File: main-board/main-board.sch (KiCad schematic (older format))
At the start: 83 parts, among them J1 C10418, J2 FH12-24S-0.5SH(55), J3 TF-01A, Q1 Q_NPN_BCE, Q2 Q_NPN_BCE, Q3 Q_NPN_BCE, Q4 DMG1012T, SW1 SW_DIP_x01, U1 ESP-32s, U2 HT7333-A, U3 CH340E, U4 DW06D, U5 IPS6404L-SQ-SPN, U6 SX1308, U7 RT9011-CMGJ6, U8 SN74LVC125ADBR

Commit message: refactor
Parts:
- removed BT1: Battery_Holder, water-lib:Battery-Holder-SMD, symbol water-lib:Battery_Holder
- removed C1, C2: 10uF, Capacitor_SMD:C_0805_2012Metric_Pad1.15x1.40mm_HandSolder, symbol Device:C
- removed C19: 1uF, Capacitor_SMD:C_0805_2012Metric_Pad1.15x1.40mm_HandSolder, symbol Device:C
- removed C3, C4, C5: 0.1uF, Capacitor_SMD:C_0805_2012Metric_Pad1.15x1.40mm_HandSolder, symbol Device:C
- removed C6, C7: 22uF, Capacitor_SMD:C_1206_3216Metric_Pad1.42x1.75mm_HandSolder, symbol Device:C
- removed D1, D2, D3, D4: LED, LED_SMD:LED_0805_2012Metric_Pad1.15x1.40mm_HandSolder, symbol Device:LED
- removed D5: D_Schottky, Diode_SMD:D_SMA_Handsoldering, symbol Device:D_Schottky
- removed F1: SMD0805-020-16V, Fuse:Fuse_0805_2012Metric_Pad1.15x1.40mm_HandSolder, symbol water-lib:SMD0805-020-16V
- removed J1: C10418, water-lib:C10418, symbol water-lib:C10418
- removed L1: 22uH, Inductor_SMD:L_Bourns-SRN6028, symbol Device:L
- removed Q1, Q2: Q_NPN_BCE, Package_TO_SOT_SMD:SOT-23, symbol Device:Q_NPN_BCE
- removed Q4: DMG1012T, water-lib:SOT-523, symbol Device:Q_NMOS_GDS
- removed R1, R2, R6: 1k, Resistor_SMD:R_0805_2012Metric_Pad1.15x1.40mm_HandSolder, symbol pspice:R
- removed R19, R20, R28, R7, R9: 10k, Resistor_SMD:R_0805_2012Metric_Pad1.15x1.40mm_HandSolder, symbol pspice:R
- removed R27: 27k, Resistor_SMD:R_0805_2012Metric_Pad1.15x1.40mm_HandSolder, symbol pspice:R
- removed R3, R4: 1k5, Resistor_SMD:R_0805_2012Metric_Pad1.15x1.40mm_HandSolder, symbol pspice:R
- removed R5: 100, Resistor_SMD:R_0805_2012Metric_Pad1.15x1.40mm_HandSolder, symbol pspice:R
- removed R8: 2k2, Resistor_SMD:R_0805_2012Metric_Pad1.15x1.40mm_HandSolder, symbol pspice:R
- removed U2: HT7333-A, Package_TO_SOT_SMD:SOT-89-3_Handsoldering, symbol water-lib:HT7333-A
- removed U3: CH340E, water-lib:CH340E-MSOP-10, symbol water-lib:CH340E
- removed U4: DW06D, Package_TO_SOT_SMD:SOT-23-6_Handsoldering, symbol water-lib:DW06D
- removed U6: SX1308, Package_TO_SOT_SMD:SOT-23-6_Handsoldering, symbol water-lib:SX1308
- renumbered C14 to C104, C16 to C105, C17 to C106, C18 to C107, C9 to C109, C15 to C110, C8 to C111, C10 to C112, C12 to C113, C11 to C114, C13 to C115, D6 to D102, H1 to H101, H2 to H102, H3 to H103, H4 to H104, J3 to J101, J2 to J102, Q3 to Q102, R14 to R106, R15 to R107, R21 to R108, R22 to R109, R23 to R110, R16 to R111, R24 to R112, R18 to R113, R25 to R116, R13 to R117, R26 to R118, R10 to R119, R11 to R120, R12 to R121, R17 to R122, SW1 to SW101, TP1 to TP101, TP2 to TP102, TP3 to TP103, TP4 to TP104, TP5 to TP105, TP6 to TP106, TP7 to TP107, U1 to U103, U8 to U104, U5 to U105, U7 to U106
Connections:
- net labels removed: CTS, D+, D-, RTS, USB_PWR
- wire segments 279 -> 175
- no-connect marks 9 -> 7
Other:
- moved on the sheet: C105, C106, J101, R108, TP101, TP102, TP103, TP104, TP105, TP106, TP107

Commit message: refactor
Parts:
- removed C105: 10uF, Capacitor_SMD:C_0805_2012Metric_Pad1.15x1.40mm_HandSolder, symbol Device:C
- removed C106, C107: 0.1uF, Capacitor_SMD:C_0805_2012Metric_Pad1.15x1.40mm_HandSolder, symbol Device:C
- removed J101: TF-01A, water-lib:TF-01A, symbol water-lib:TF-01A
- removed R108, R109, R110, R112: 3k3, Resistor_SMD:R_0805_2012Metric_Pad1.15x1.40mm_HandSolder, symbol pspice:R
- removed TP102: VBAT, TestPoint:TestPoint_Pad_D1.0mm, symbol Connector:TestPoint
- removed U104: SN74LVC125ADBR, Package_SO:TSSOP-14_4.4x5mm_P0.65mm, symbol water-lib:SN74LVC125ADBR
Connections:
- net labels removed: SD_CLK, SD_CMD, SD_D0, SD_D3, VBAT
- wire segments 175 -> 134
- no-connect marks 7 -> 6
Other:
- moved on the sheet: D102, H101, H102, H103, H104, Q102, R113, R116, R118, SW101, TP101, TP103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

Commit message: ALPHA 1
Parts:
- removed C109, C110, C112, C114: 1uF, Capacitor_SMD:C_0805_2012Metric_Pad1.15x1.40mm_HandSolder, symbol Device:C
- removed C113: 15pF, Capacitor_SMD:C_0805_2012Metric_Pad1.15x1.40mm_HandSolder, symbol Device:C
- removed C115: 0.1uF, Capacitor_SMD:C_0805_2012Metric_Pad1.15x1.40mm_HandSolder, symbol Device:C
- removed J102: FH12-24S-0.5SH(55), water-lib:FH12-24S-0.5SH(55), symbol water-lib:FH12-24S-0.5SH(55)
- removed R106, R107, R122: 4k7, Resistor_SMD:R_0805_2012Metric_Pad1.15x1.40mm_HandSolder, symbol pspice:R
- removed R111, R120, R121: 10k, Resistor_SMD:R_0805_2012Metric_Pad1.15x1.40mm_HandSolder, symbol pspice:R
- removed R117: 1k, Resistor_SMD:R_0805_2012Metric_Pad1.15x1.40mm_HandSolder, symbol pspice:R
- removed U106: RT9011-CMGJ6, Package_TO_SOT_SMD:SOT-23-6_Handsoldering, symbol water-lib:RT9011-CMGJ6
- SW101: value SW_DIP_x01 -> RESET
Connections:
- net labels removed: CAM_RST, CSI_PWD
- wire segments 134 -> 90
- no-connect marks 6 -> 3
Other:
- moved on the sheet: C104, C111, D102, H101, H102, H103, H104, Q102, R113, R116, R118, R119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

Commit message: ALPHA 1
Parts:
- removed TP101: +2V8, TestPoint:TestPoint_Pad_D1.0mm, symbol Connector:TestPoint
- removed TP104: +5V, TestPoint:TestPoint_Pad_D1.0mm, symbol Connector:TestPoint
- removed TP105: +3.3V, TestPoint:TestPoint_Pad_D1.0mm, symbol Connector:TestPoint
- removed TP106: +3V3, TestPoint:TestPoint_Pad_D1.0mm, symbol Connector:TestPoint
- removed TP107: +1V2, TestPoint:TestPoint_Pad_D1.0mm, symbol Connector:TestPoint
- renumbered C104 to C101, C111 to C102, D102 to D101, Q102 to Q101, R116 to R101, R113 to R102, R118 to R103, R119 to R104, TP103 to TP101, U103 to U101, U105 to U102
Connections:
- net labels removed: +1V2, +2V8, +5V, VCC
- wire segments 90 -> 85
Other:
- moved on the sheet: TP101
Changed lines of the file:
@@
 $EndDescr
 $Comp
-L water-lib:ESP-32s U103
+L water-lib:ESP-32s U101
 U 1 1 5D945085
 P 5240 1280
-F 0 "U103" H 5990 1545 50  0000 C CNN
+F 0 "U101" H 5990 1545 50  0000 C CNN
 F 1 "ESP-32s" H 5990 1454 50  0000 C CNN
 F 2 "water-lib:ESP-32S" H 6590 1380 50  0001 L CNN
@@
 $EndComp
 $Comp
-L water-lib:IPS6404L-SQ-SPN U105
+L water-lib:IPS6404L-SQ-SPN U102
 U 1 1 5D96C0DE
 P 9430 2160
-F 0 "U105" H 9455 2535 50  0000 C CNN
+F 0 "U102" H 9455 2535 50  0000 C CNN
 F 1 "IPS6404L-SQ-SPN" H 9455 2444 50  0000 C CNN
 F 2 "Package_SO:SOP-8_3.76x4.96mm_P1.27mm" H 9430 1860 50  0001 C CNN
@@
 SD1
 $Comp
-L power:GND #PWR0136
+L power:GND #PWR0111
 U 1 1 5D9B56A0
 P 9030 2470
-F 0 "#PWR0136" H 9030 2220 50  0001 C CNN
+F 0 "#PWR0111" H 9030 2220 50  0001 C CNN
 F 1 "GND" H 9035 2297 50  0000 C CNN
 F 2 "" H 9030 2470 50  0001 C CNN
@@
 	9030 2310 9030 2470
 $Comp
-L pspice:R R119
+L pspice:R R104
 U 1 1 5D9B9656
 P 8740 1760
-F 0 "R119" V 8640 1760 50  0000 C CNN
+F 0 "R104" V 8640 1760 50  0000 C CNN
 F 1 "10k" V 8740 1760 50  0000 C CNN
 F 2 "Resistor_SMD:R_0805_2012Metric_Pad1.15x1.40mm_HandSolder" H 8740 1760 50  0001 C CNN
@@
 $EndComp
 $Comp
-L power:+3V3 #PWR0134
+L power:+3V3 #PWR0110
 U 1 1 5D9BA596
 P 8740 1470
-F 0 "#PWR0134" H 8740 1320 50  0001 C CNN
+F 0 "#PWR0110" H 8740 1320 50  0001 C CNN
 F 1 "+3V3" H 8755 1643 50  0000 C CNN
 F 2 "" H 8740 1470 50  0001 C CNN
@@
 	8740 1470 8740 1510
 $Comp
-L Device:C C111
+L Device:C C102
 U 1 1 5D9BE3F5
 P 10110 1840
-F 0 "C111" H 9980 1930 50  0000 L CNN
+F 0 "C102" H 9980 1930 50  0000 L CNN
 F 1 "1uF" H 9880 1760 50  0000 L CNN
 F 2 "Capacitor_SMD:C_0805_2012Metric_Pad1.15x1.40mm_HandSolder" H 10148 1690 50  0001 C CNN
@@
 $EndComp
 $Comp
-L power:+3V3 #PWR0140
+L power:+3V3 #PWR0112
 U 1 1 5D9BFF85
 P 9960 1600
-F 0 "#PWR0140" H 9960 1450 50  0001 C CNN
+F 0 "#PWR0112" H 9960 1450 50  0001 C CNN
 F 1 "+3V3" H 9975 1773 50  0000 C CNN
 F 2 "" H 9960 1600 50  0001 C CNN
@@
 $EndComp
 $Comp
-L power:GND #PWR0142
+L power:GND #PWR0113
 U 1 1 5D9C0676
 P 10340 1840
-F 0 "#PWR0142" H 10340 1590 50  0001 C CNN
+F 0 "#PWR0113" H 10340 1590 50  0001 C CNN
 F 1 "GND" H 10345 1667 50  0000 C CNN
 F 2 "" H 10340 1840 50  0001 C CNN
@@
 CSI_PCLK
 $Comp
-L power:GND #PWR0118
+L power:GND #PWR0107
 U 1 1 5DBD9981
 P 5030 1080
-F 0 "#PWR0118" H 5030 830 50  0001 C CNN
+F 0 "#PWR0107" H 5030 830 50  0001 C CNN
 F 1 "GND" H 5035 907 50  0000 C CNN
 F 2 "" H 5030 1080 50  0001 C CNN
@@
 	5030 1080 5240 1080
 $Comp
-L Device:CP C104
+L Device:CP C101
 U 1 1 5DBF5EA7
 P 4830 1230
-F 0 "C104" H 4712 1184 50  0000 R CNN
+F 0 "C101" H 4712 1184 50  0000 R CNN
 F 1 "100uF" H 4712 1275 50  0000 R CNN
 F 2 "water-lib:TAJB107M010RNJ" H 4868 1080 50  0001 C CNN
@@
 CSI_MCLK
 $Comp
-L power:+3V3 #PWR0116
+L power:+3V3 #PWR0106
 U 1 1 5DC38360
 P 4610 1380
-F 0 "#PWR0116" H 4610 1230 50  0001 C CNN
+F 0 "#PWR0106" H 4610 1230 50  0001 C CNN
 F 1 "+3V3" H 4625 1553 50  0000 C CNN
 F 2 "" H 4610 1380 50  0001 C CNN
@@
 $EndComp
 $Comp
-L power:GND #PWR0123
+L power:GND #PWR0102
 U 1 1 5DA3B5A0
 P 2390 1350
-F 0 "#PWR0123" H 2390 1100 50  0001 C CNN
+F 0 "#PWR0102" H 2390 1100 50  0001 C CNN
 F 1 "GND" H 2395 1177 50  0000 C CNN
 F 2 "" H 2390 1350 50  0001 C CNN
@@
 	3330 1350 3760 1350
 $Comp
-L power:+3V3 #PWR0126
+L power:+3V3 #PWR0103
 U 1 1 5DA640C1
 P 3330 790
-F 0 "#PWR0126" H 3330 640 50  0001 C CNN
+F 0 "#PWR0103" H 3330 640 50  0001 C CNN
 F 1 "+3V3" H 3345 963 50  0000 C CNN
 F 2 "" H 3330 790 50  0001 C CNN
@@
 IO0
 $Comp
-L Device:Q_NPN_BCE Q102
+L Device:Q_NPN_BCE Q101
 U 1 1 5D9D459B
 P 3240 2440
-F 0 "Q102" H 3431 2486 50  0000 L CNN
+F 0 "Q101" H 3431 2486 50  0000 L CNN
 F 1 "Q_NPN_BCE" H 3431 2395 50  0000 L CNN
 F 2 "Package_TO_SOT_SMD:SOT-23" H 3440 2540 50  0001 C CNN
@@
 NoConn ~ 6740 2480
 $Comp
-L power:GND #PWR0121
+L power:GND #PWR0109
 U 1 1 5D9E8C86
 P 6780 3080
-F 0 "#PWR0121" H 6780 2830 50  0001 C CNN
+F 0 "#PWR0109" H 6780 2830 50  0001 C CNN
 F 1 "GND" H 6785 2907 50  0000 C CNN
 F 2 "" H 6780 3080 50  0001 C CNN
@@
 	6740 3080 6780 3080
 $Comp
-L power:GND #PWR0119
+L power:GND #PWR0108
 U 1 1 5D9FCC82
 P 5210 2680
-F 0 "#PWR0119" H 5210 2430 50  0001 C CNN
+F 0 "#PWR0108" H 5210 2430 50  0001 C CNN
 F 1 "GND" H 5215 2507 50  0000 C CNN
 F 2 "" H 5210 2680 50  0001 C CNN
@@
 IO13
 $Comp
-L pspice:R R116
+L pspice:R R101
 U 1 1 5DA399B3
 P 2740 2440
-F 0 "R116" V 2820 2440 50  0000 C CNN
+F 0 "R101" V 2820 2440 50  0000 C CNN
 F 1 "1k" V 2740 2440 50  0000 C CNN
 F 2 "Resistor_SMD:R_0805_2012Metric_Pad1.15x1.40mm_HandSolder" H 2740 2440 50  0001 C CNN
@@
 IO13
 $Comp
-L pspice:R R118
+L pspice:R R103
 U 1 1 5DA790E1
 P 3340 2960
-F 0 "R118" V 3420 2960 50  0000 C CNN
+F 0 "R103" V 3420 2960 50  0000 C CNN
 F 1 "1k" V 3340 2960 50  0000 C CNN
 F 2 "Resistor_SMD:R_0805_2012Metric_Pad1.15x1.40mm_HandSolder" H 3340 2960 50  0001 C CNN
@@
 $EndComp
 $Comp
-L power:GND #PWR0133
+L power:GND #PWR0105
 U 1 1 5DA7A289
 P 3340 3280
-F 0 "#PWR0133" H 3340 3030 50  0001 C CNN
+F 0 "#PWR0105" H 3340 3030 50  0001 C CNN
 F 1 "GND" H 3345 3107 50  0000 C CNN
 F 2 "" H 3340 3280 50  0001 C CNN
@@
 $EndComp
 $Comp
-L power:+3V3 #PWR0132
+L power:+3V3 #PWR0104
 U 1 1 5DA7CA61
 P 3340 1770
-F 0 "#PWR0132" H 3340 1620 50  0001 C CNN
+F 0 "#PWR0104" H 3340 1620 50  0001 C CNN
 F 1 "+3V3" H 3355 1943 50  0000 C CNN
 F 2 "" H 3340 1770 50  0001 C CNN
@@
 IO32
 $Comp
-L water-lib:HQ67-2100IRC D102
+L water-lib:HQ67-2100IRC D101
 U 1 1 5DD8FA79
 P 3340 1990
-F 0 "D102" V 3379 1873 50  0000 R CNN
+F 0 "D101" V 3379 1873 50  0000 R CNN
 F 1 "HQ67-2100IRC" V 3288 1873 50  0000 R CNN
 F 2 "water-lib:HQ67-2100IRC" H 3340 1640 50  0001 C CNN
@@
 $EndComp
 $Comp
-L Connector:TestPoint TP103
+L Connector:TestPoint TP101
 U 1 1 5DA2FB24
-P 1510 6260
-F 0 "TP103" V 1580 6430 50  0000 R CNN
-F 1 "GND" V 1420 6430 50  0000 R CNN
-F 2 "TestPoint:TestPoint_Pad_D1.0mm" H 1710 6260 50  0001 C CNN
-F 3 "~" H 1710 6260 50  0001 C CNN
-	1    1510 6260
-	0    -1   -1   0
-$EndComp
-$Comp
-L Connector:TestPoint TP104
-U 1 1 5DA9028F
-P 1510 6540
-F 0 "TP104" V 1580 6710 50  0000 R CNN
-F 1 "+5V" V 1420 6710 50  0000 R CNN
-F 2 "TestPoint:TestPoint_Pad_D1.0mm" H 1710 6540 50  0001 C CNN
-F 3 "~" H 1710 6540 50  0001 C CNN
-	1    1510 6540
-	0    -1   -1   0
-$EndComp
-$Comp
-L Connector:TestPoint TP105
-U 1 1 5DA90A60
-P 1510 6810
-F 0 "TP105" V 1580 6980 50  0000 R CNN
-F 1 "+3.3V" V 1420 6980 50  0000 R CNN
-F 2 "TestPoint:TestPoint_Pad_D1.0mm" H 1710 6810 50  0001 C CNN
-F 3 "~" H 1710 6810 50  0001 C CNN
-	1    1510 6810
-	0    -1   -1   0
-$EndComp
-$Comp
-L Connector:TestPoint TP106
-U 1 1 5DA90FD1
-P 1510 7070
-F 0 "TP106" V 1580 7240 50  0000 R CNN
-F 1 "+3V3" V 1420 7240 50  0000 R CNN
-F 2 "TestPoint:TestPoint_Pad_D1.0mm" H 1710 7070 50  0001 C CNN
-F 3 "~" H 1710 7070 50  0001 C CNN
-	1    1510 7070
-	0    -1   -1   0
-$EndComp
-$Comp
-L Connector:TestPoint TP107
-U 1 1 5DA913A0
-P 1510 7360
-F 0 "TP107" V 1580 7530 50  0000 R CNN
-F 1 "+1V2" V 1420 7530 50  0000 R CNN
-F 2 "TestPoint:TestPoint_Pad_D1.0mm" H 1710 7360 50  0001 C CNN
-F 3 "~" H 1710 7360 50  0001 C CNN
-	1    1510 7360
+P 740 6620
+F 0 "TP101" V 810 6790 50  0000 R CNN
+F 1 "GND" V 650 6790 50  0000 R CNN
+F 2 "TestPoint:TestPoint_Pad_D1.0mm" H 940 6620 50  0001 C CNN
+F 3 "~" H 940 6620 50  0001 C CNN
+	1    740  6620
 	0    -1   -1   0
 $EndComp
@@
 L power:GND #PWR0101
 U 1 1 5DA91749
-P 1560 6260
-F 0 "#PWR0101" H 1560 6010 50  0001 C CNN
-F 1 "GND" H 1565 6087 50  0000 C CNN
-F 2 "" H 1560 6260 50  0001 C CNN
-F 3 "" H 1560 6260 50  0001 C CNN
-	1    1560 6260
+P 790 6620
+F 0 "#PWR0101" H 790 6370 50  0001 C CNN
+F 1 "GND" H 795 6447 50  0000 C CNN
+F 2 "" H 790 6620 50  0001 C CNN
+F 3 "" H 790 6620 50  0001 C CNN
+	1    790  6620
 	0    -1   -1   0
 $EndComp
-$Comp
-L power:+5V #PWR0102
-U 1 1 5DA92174
-P 1560 6540
-F 0 "#PWR0102" H 1560 6390 50  0001 C CNN
-F 1 "+5V" H 1575 6713 50  0000 C CNN
-F 2 "" H 1560 6540 50  0001 C CNN
-F 3 "" H 1560 6540 50  0001 C CNN
-	1    1560 6540
-	0    1    1    0
-$EndComp
-$Comp
-L power:VCC #PWR0103
-U 1 1 5DA9346E
-P 1580 6810
-F 0 "#PWR0103" H 1580 6660 50  0001 C CNN
-F 1 "VCC" H 1597 6983 50  0000 C CNN
-F 2 "" H 1580 6810 50  0001 C CNN
-F 3 "" H 1580 6810 50  0001 C CNN
-	1    1580 6810
-	0    1    1    0
-$EndComp
-$Comp
-L power:+3V3 #PWR0104
-U 1 1 5DA94330
-P 1590 7070
-F 0 "#PWR0104" H 1590 6920 50  0001 C CNN
-F 1 "+3V3" H 1605 7243 50  0000 C CNN
-F 2 "" H 1590 7070 50  0001 C CNN
-F 3 "" H 1590 7070 50  0001 C CNN
-	1    1590 7070
-	0    1    1    0
-$EndComp
-$Comp
-L power:+1V2 #PWR0105
-U 1 1 5DA9596A
-P 1610 7360
-F 0 "#PWR0105" H 1610 7210 50  0001 C CNN
-F 1 "+1V2" H 1625 7533 50  0000 C CNN
-F 2 "" H 1610 7360 50  0001 C CNN
-F 3 "" H 1610 7360 50  0001 C CNN
-	1    1610 7360
-	0    1    1    0
-$EndComp
-$Comp
-L Connector:TestPoint TP101
-U 1 1 5DA972FE
-P 1500 7630
-F 0 "TP101" V 1570 7800 50  0000 R CNN
-F 1 "+2V8" V 1410 7800 50  0000 R CNN
-F 2 "TestPoint:TestPoint_Pad_D1.0mm" H 1700 7630 50  0001 C CNN
-F 3 "~" H 1700 7630 50  0001 C CNN
-	1    1500 7630
-	0    -1   -1   0
-$EndComp
-$Comp
-L power:+2V8 #PWR0106
-U 1 1 5DA979D8
-P 1610 7630
-F 0 "#PWR0106" H 1610 7480 50  0001 C CNN
-F 1 "+2V8" H 1625 7803 50  0000 C CNN
-F 2 "" H 1610 7630 50  0001 C CNN
-F 3 "" H 1610 7630 50  0001 C CNN
-	1    1610 7630
-	0    1    1    0
-$EndComp
-Wire Wire Line
-	1510 6260 1560 6260
-Wire Wire Line
-	1510 6540 1560 6540
-Wire Wire Line
-	1510 6810 1580 6810
-Wire Wire Line
-	1510 7070 1590 7070
-Wire Wire Line
-	1510 7360 1610 7360
-Wire Wire Line
-	1500 7630 1610 7630
+Wire Wire Line
+	740  6620 790  6620
 Wire Wire Line
 	1580 1990 1750 1990
@@
 IO32
 $Comp
-L pspice:R R113
+L pspice:R R102
 U 1 1 5DA63BFF
 P 3330 1100
-F 0 "R113" V 3230 1100 50  0000 C CNN
+F 0 "R102" V 3230 1100 50  0000 C CNN
 F 1 "10k" V 3330 1100 50  0000 C CNN
 F 2 "Resistor_SMD:R_0805_2012Metric_Pad1.15x1.40mm_HandSolder" H 3330 1100 50  0001 C CNN

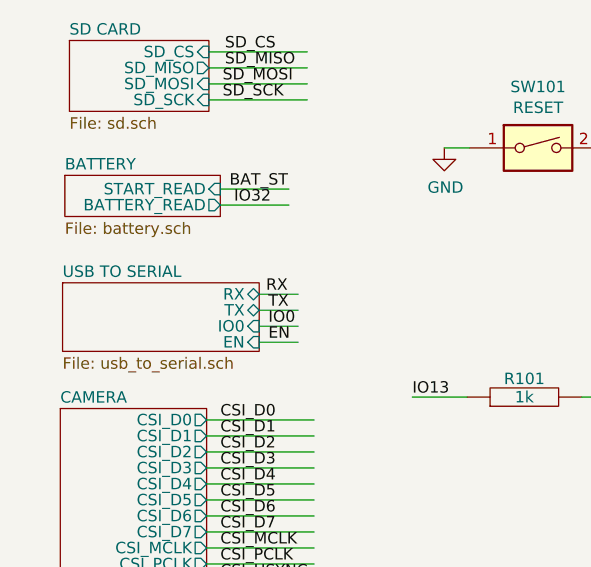
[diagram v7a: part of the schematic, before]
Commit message: added battery charging
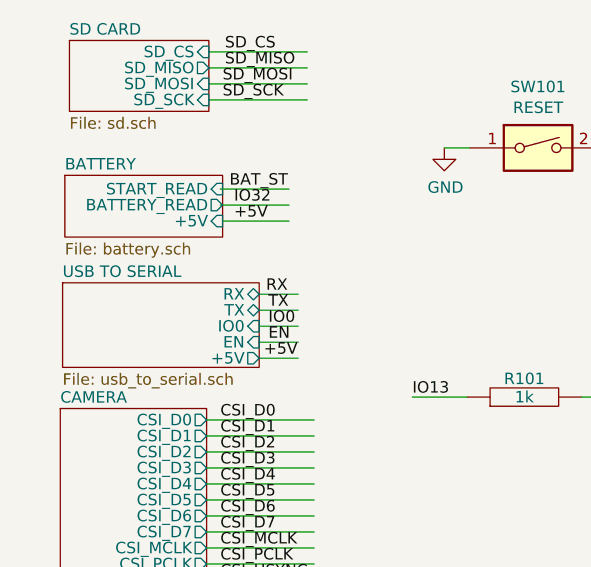
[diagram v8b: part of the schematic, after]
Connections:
- net labels added: +5V
- wire segments 85 -> 87
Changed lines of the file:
@@
 	1580 1990 1750 1990
 $Sheet
-S 720  1940 860  300
+S 720  1940 860  370
 U 5DA658CB
 F0 "USB TO SERIAL" 50
@@
 F4 "IO0" I R 1580 2130 50
 F5 "EN" I R 1580 2200 50
+F6 "+5V" O R 1580 2270 50
 $EndSheet
 Wire Wire Line
@@
 $EndSheet
 $Sheet
-S 730  1470 680  180
+S 730  1470 690  270
 U 5DC2722E
 F0 "BATTERY" 50
 F1 "battery.sch" 50
-F2 "START_READ" I R 1410 1530 50
-F3 "BATTERY_READ" O R 1410 1600 50
+F2 "START_READ" I R 1420 1530 50
+F3 "BATTERY_READ" O R 1420 1600 50
+F4 "+5V" I R 1420 1670 50
 $EndSheet
 Wire Wire Line
@@
 Wire Wire Line
 	1350 3310 1820 3310
+Wire Wire Line
+	1580 2270 1750 2270
+Text Label 1600 2270 0    50   ~ 0
++5V
+Wire Wire Line
+	1420 1670 1710 1670
+Text Label 1470 1670 0    50   ~ 0
++5V
 $EndSCHEMATC
